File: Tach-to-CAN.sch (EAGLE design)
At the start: 51 parts, among them J1 CONN_4PIN_VERT, J2 CONN_4PIN_VERT, Q1 NXP_NX3008NBK,215NXP_SOT23, Q2 8MHz, U1 VISHAY_VOMA618A-2X001T, U3 TI_TPS7A1633AQDGNRQ1, U4 STM32F303K8T6STMICROELECTRONI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

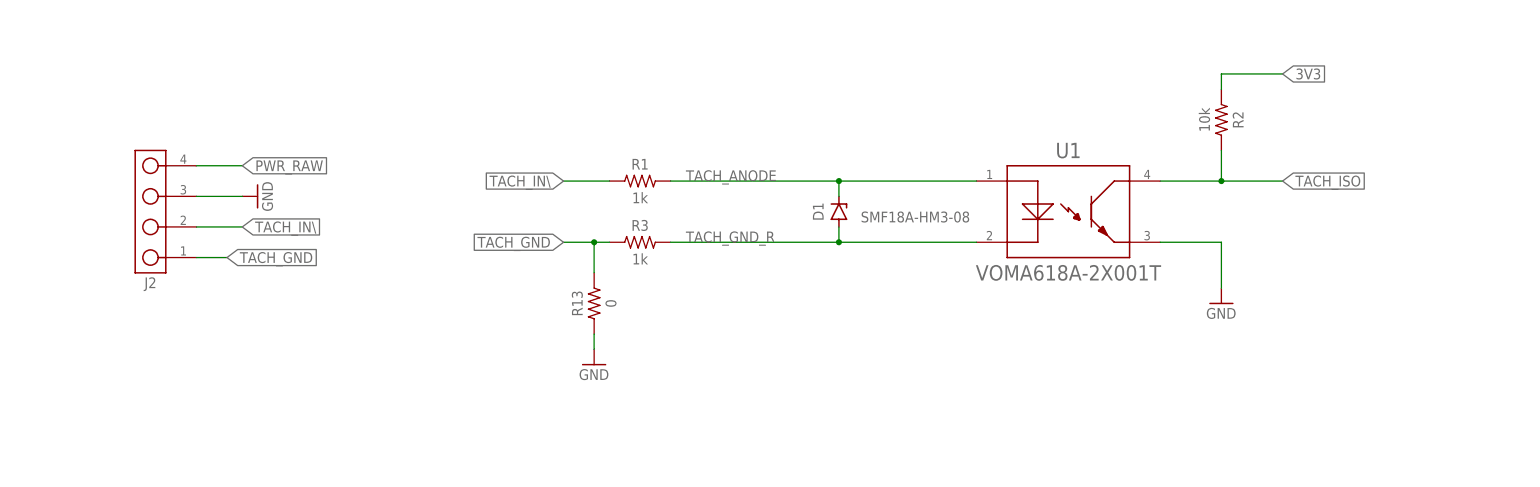
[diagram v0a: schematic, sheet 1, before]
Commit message: Add NFET to buffer TACH_IN signal
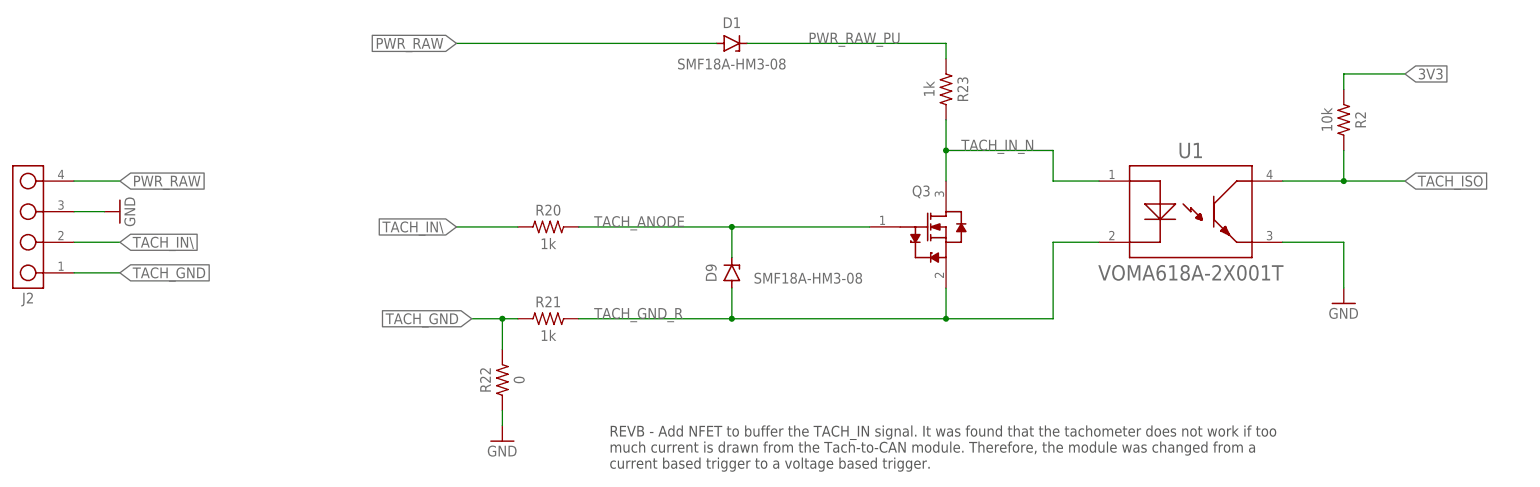
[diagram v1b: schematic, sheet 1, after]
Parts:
- removed R1, R3: 1k, resistors:1KOHM-0603-1%-1/10W
- removed R13: 0, resistors:0OHM-0603-1%-1/10W
- added D9: VISHAY_SMF18A-HM3-08, AlphaLibrary:VISHAY_SMF18A-HM3-08
- added Q3: NEXPERIA_PMV60ENEAR, AlphaLibrary:NEXPERIA_PMV60ENEAR
- added R20, R21, R23: 1k, resistors:1KOHM-0603-1%-1/10W
- added R22: 0, resistors:0OHM-0603-1%-1/10W
- U2: value (none) -> TI_SN65HVD23X
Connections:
- new net PWR_RAW_PU: D1.C, R23.1
- new net TACH_IN_N: Q3.D, R23.2, U1.1
- net GND: now also R22.1; no longer R13.1
- net PWR_RAW: now also D1.A
- net TACH_ANODE: now also D9.C, Q3.G, R20.2; no longer D1.C, R1.2, U1.1
- net TACH_GND: now also R21.1, R22.2; no longer R13.2, R3.1
- net TACH_GND_R: now also D9.A, Q3.S, R21.2; no longer D1.A, R3.2
- net TACH_IN\: now also R20.1; no longer R1.1
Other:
- note added: "REVB - Add NFET to buffer the TACH_IN signal. It was found that the tachometer does not work if too much current is drawn from the Tach-to-CAN module. Therefore, the module was changed from a current based trigger to a voltage based trigger."
- moved on the sheet: D1, J2, R2, U1
